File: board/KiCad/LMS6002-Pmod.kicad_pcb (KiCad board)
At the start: 2 copper layers, 30.5 x 29.2 mm, 3 parts, among them P1 PMOD_2x6, P2 PMOD_2x6, U1 iCE40_1K4K_TQ144

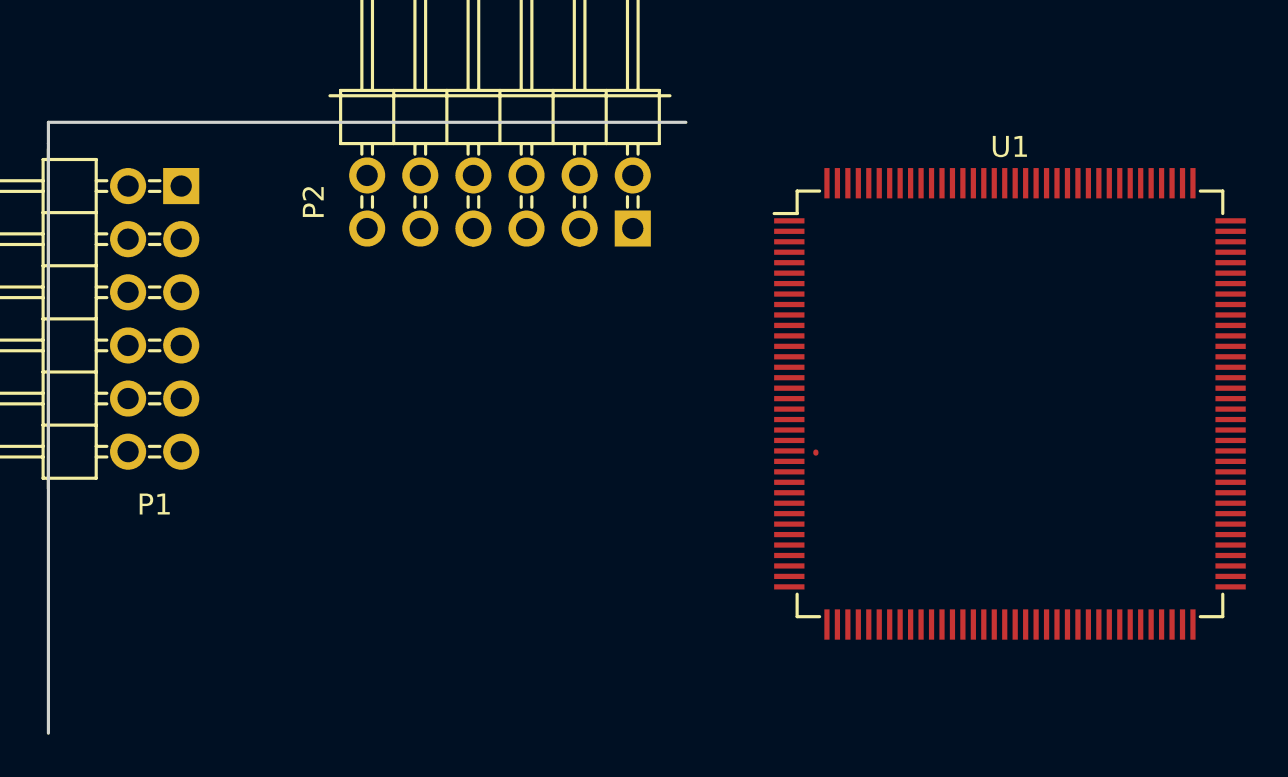
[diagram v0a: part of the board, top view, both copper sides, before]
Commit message: pmod wiring
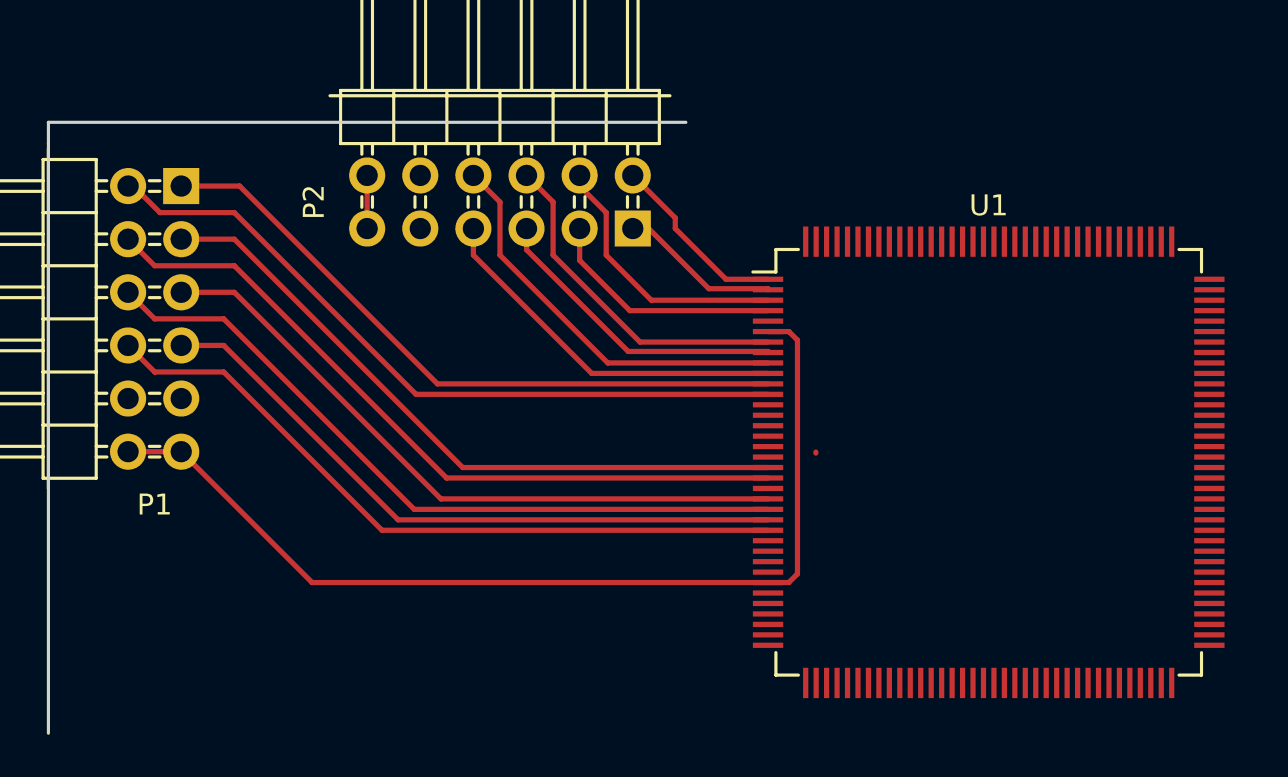
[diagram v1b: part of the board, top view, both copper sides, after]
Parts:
- moved U1 2.97 mm to (133.9, 101.1)
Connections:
- U1 pad 30: Net-(U1-Pad30) -> +3V3
- U1 pad 6: Net-(U1-Pad6) -> +3V3
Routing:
- net +3V3: track 0.00 -> 50.1 mm
- net PIO5: track 0.00 -> 35.3 mm
- net PIO6: track 0.00 -> 34.9 mm
- net PIO4: track 0.00 -> 34.7 mm
- net PIO7: track 0.00 -> 34.3 mm
- net PIO1: track 0.00 -> 32.6 mm
- net PIO2: track 0.00 -> 32.1 mm
- net PIO0: track 0.00 -> 32.0 mm
- net PIO3: track 0.00 -> 31.5 mm
- net PIO15: track 0.00 -> 19.3 mm
- net PIO11: track 0.76 -> 18.5 mm
- net PIO14: track 0.00 -> 16.3 mm
- net PIO10: track 0.64 -> 15.3 mm
- net PIO13: track 0.25 -> 13.2 mm
- net PIO9: track 0.76 -> 12.3 mm
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
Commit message: Finalize first draft
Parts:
- added C1: 10µF, Capacitors_SMD:C_0603_HandSoldering, F.Cu at (117.5, 112.2)
- added C10: 10µF, Capacitors_SMD:C_0603_HandSoldering, B.Cu at (126.8, 96.3)
- added C11: 1µF, Capacitors_SMD:C_0603_HandSoldering, B.Cu at (128.6, 96.3)
- added C12: 0.1µF, Capacitors_SMD:C_0603_HandSoldering, B.Cu at (130.4, 96.3)
- added C13: 0.01µF, Capacitors_SMD:C_0603_HandSoldering, B.Cu at (124.9, 96.3)
- added C14: 100n, Capacitors_SMD:C_0603_HandSoldering, B.Cu at (140.4, 105.8)
- added C15: 100n, Capacitors_SMD:C_0603_HandSoldering, B.Cu at (122.8, 93.9)
- added C16: 100n, Capacitors_SMD:C_0603_HandSoldering, F.Cu at (128.8, 115.3)
- added C17: 100n, Capacitors_SMD:C_0603_HandSoldering, B.Cu at (119.7, 108.7)
- added C18: 100n, Capacitors_SMD:C_0603_HandSoldering, B.Cu at (142.9, 103.7)
- added C19: 100n, Capacitors_SMD:C_0603_HandSoldering, B.Cu at (138.1, 95.9)
- added C2: 0.1µF, Capacitors_SMD:C_0603_HandSoldering, F.Cu at (115.7, 112.2)
- added C20: 100n, Capacitors_SMD:C_0603_HandSoldering, F.Cu at (140.5, 89.6)
- added C21: 100n, Capacitors_SMD:C_0603_HandSoldering, F.Cu at (134.2, 89.6)
- added C22: 100n, Capacitors_SMD:C_0603_HandSoldering, F.Cu at (118.5, 107.7)
- added C23: 100n, Capacitors_SMD:C_0603_HandSoldering, B.Cu at (126.7, 91.5)
- added C3: 1µF, Capacitors_Tantalum_SMD:TantalC_SizeA_EIA-3216_HandSoldering, B.Cu at (109.1, 97.7)
- added C4: 1µF, Capacitors_Tantalum_SMD:TantalC_SizeA_EIA-3216_HandSoldering, B.Cu at (116.8, 109.7)
- added C5: 0.1µ, Capacitors_SMD:C_0603_HandSoldering, B.Cu at (116.3, 102.0)
- added C6: 10µF, Capacitors_SMD:C_0603_HandSoldering, B.Cu at (126.8, 100.5)
- added C7: 1µF, Capacitors_SMD:C_0603_HandSoldering, B.Cu at (128.6, 100.5)
- added C8: 0.1µF, Capacitors_SMD:C_0603_HandSoldering, B.Cu at (124.9, 100.5)
- added C9: 0.01µF, Capacitors_SMD:C_0603_HandSoldering, B.Cu at (130.4, 100.5)
- added CON1: BARREL_JACK, Connect:BARREL_JACK, F.Cu at (105.2, 114.0)
- added D1: 5V-SOD-123F, pmod:SOD-123F_Handsoldering, B.Cu at (96.3, 114.9)
- added D2: Schottky 0520, pmod:SOD-123_Handsoldering, F.Cu at (140.2, 87.6)
- added D3: LED, SMD_Packages:SMD-1206_Pol, F.Cu at (132.8, 87.3)
- added D4: LED, SMD_Packages:SMD-1206_Pol, F.Cu at (127.0, 87.3)
- added D5: LED, SMD_Packages:SMD-1206_Pol, F.Cu at (121.3, 87.3)
- added D6: LED, SMD_Packages:SMD-1206_Pol, F.Cu at (133.0, 119.0)
- added F1: 2A-0603, Capacitors_SMD:C_0603_HandSoldering, B.Cu at (97.4, 107.6)
- added J1: FX10B_80S_8, pmod:FX10B_80S_8, F.Cu at (151.4, 103.0)
- added J2: Pinheader_1x6_TH, Pin_Headers:Pin_Header_Straight_1x06, F.Cu at (113.7, 118.8)
- added J3: SELECT_DIV, Pin_Headers:Pin_Header_Straight_1x03, F.Cu at (104.6, 102.4)
- added JP1: LDO_1V2_IN_SEL, Pin_Headers:Pin_Header_Straight_1x03, F.Cu at (92.3, 112.6)
- added Q1: IRLML6344bpf, TO_SOT_Packages_SMD:SOT-23_Handsoldering, B.Cu at (99.7, 112.0)
- added R1: 100, Resistors_SMD:R_0603_HandSoldering, F.Cu at (113.7, 106.4)
- added R10: 10k, Resistors_SMD:R_0603_HandSoldering, B.Cu at (135.3, 104.3)
- added R11: 10k, Resistors_SMD:R_0603_HandSoldering, F.Cu at (143.3, 115.1)
- added R12: 10K, Resistors_SMD:R_0603_HandSoldering, F.Cu at (143.3, 117.0)
- added R2: 10, Resistors_SMD:R_0603_HandSoldering, F.Cu at (129.0, 89.5)
- added R3: 10, Resistors_SMD:R_0603_HandSoldering, F.Cu at (124.6, 89.5)
- added R4: 10, Resistors_SMD:R_0603_HandSoldering, F.Cu at (120.0, 89.6)
- added R5: R, Resistors_SMD:R_0603_HandSoldering, B.Cu at (112.4, 98.0)
- added R6: 10k, Resistors_SMD:R_0603_HandSoldering, B.Cu at (124.9, 109.2)
- added R7: 10K, Resistors_SMD:R_0603_HandSoldering, F.Cu at (139.0, 116.2)
- added R8: 10, Resistors_SMD:R_0603_HandSoldering, F.Cu at (134.6, 116.2)
- added R9: 10k, Resistors_SMD:R_0603_HandSoldering, B.Cu at (125.0, 104.8)
- added SW1: ICE_RESET, pmod:B3U-1000P_Handsoldering, F.Cu at (141.9, 119.7)
- added U2: LD6815, pmod:SOT-753_(TSOP-5)_Handsoldering, B.Cu at (111.1, 104.4)
- added U3: LTC1799, pmod:TSOT-23_Handsoldering, B.Cu at (117.9, 98.0)
- added U4: N25Q, pmod:SOP2-8_Handsoldering, B.Cu at (131.9, 108.0)
- moved U1 2.57 mm to (131.7, 102.5)
- moved P2 1.61 mm to (116.6, 83.0)
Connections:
- P1 pad 12: +3V3 -> 3V3_PMOD
- P1 pad 6: +3V3 -> 3V3_PMOD
- P2 pad 12: +3V3 -> 3V3_PMOD
- P2 pad 6: +3V3 -> 3V3_PMOD
- U1 pad 100: Net-(U1-Pad100) -> 3V3_PMOD
- U1 pad 101: Net-(U1-Pad101) -> FCLK2
- U1 pad 102: Net-(U1-Pad102) -> RFDIO_GPIO0
- U1 pad 103: Net-(U1-Pad103) -> GND
- U1 pad 104: Net-(U1-Pad104) -> RFDIO_GPIO1
- U1 pad 105: Net-(U1-Pad105) -> RFDIO_GPIO2
- U1 pad 106: Net-(U1-Pad106) -> RFDIO_REF_CLK_IN
- U1 pad 107: Net-(U1-Pad107) -> TXEN
- U1 pad 108: Net-(U1-Pad108) -> (no net)
- U1 pad 110: Net-(U1-Pad110) -> (no net)
- U1 pad 111: Net-(U1-Pad111) -> 1V2_LDO
- U1 pad 112: Net-(U1-Pad112) -> RXEN
- U1 pad 113: Net-(U1-Pad113) -> RFDIO_SPI_EN
- U1 pad 114: Net-(U1-Pad114) -> RFDIO_SPI_CLK
- U1 pad 115: Net-(U1-Pad115) -> RFDIO_SPI_MISO
- U1 pad 116: Net-(U1-Pad116) -> RFDIO_SPI_MOSI
- U1 pad 117: Net-(U1-Pad117) -> RFDIO_RESET
- U1 pad 118: Net-(U1-Pad118) -> FCLK1
- U1 pad 119: Net-(U1-Pad119) -> DIQ2_D11
- U1 pad 120: Net-(U1-Pad120) -> DIQ2_D9
- U1 pad 121: Net-(U1-Pad121) -> DIQ2_D7
- U1 pad 122: Net-(U1-Pad122) -> DIQ2_D5
- U1 pad 123: Net-(U1-Pad123) -> 3V3_PMOD
- U1 pad 124: Net-(U1-Pad124) -> (no net)
- U1 pad 125: Net-(U1-Pad125) -> (no net)
- U1 pad 126: Net-(U1-Pad126) -> (no net)
- U1 pad 127: Net-(U1-Pad127) -> (no net)
- U1 pad 128: Net-(U1-Pad128) -> DIQ2_D3
- U1 pad 129: Net-(U1-Pad129) -> DIQ2_D1
- U1 pad 13: Net-(U1-Pad13) -> GND
- U1 pad 130: Net-(U1-Pad130) -> (no net)
- U1 pad 131: Net-(U1-Pad131) -> (no net)
- U1 pad 132: Net-(U1-Pad132) -> GND
- U1 pad 133: Net-(U1-Pad133) -> 3V3_PMOD
- U1 pad 134: Net-(U1-Pad134) -> DIQ1_D11
- U1 pad 135: Net-(U1-Pad135) -> (no net)
- U1 pad 136: Net-(U1-Pad136) -> (no net)
- U1 pad 137: Net-(U1-Pad137) -> (no net)
- U1 pad 138: Net-(U1-Pad138) -> (no net)
- U1 pad 139: Net-(U1-Pad139) -> (no net)
- U1 pad 14: Net-(U1-Pad14) -> GND
- U1 pad 140: Net-(U1-Pad140) -> GND
- U1 pad 141: Net-(U1-Pad141) -> (no net)
- U1 pad 15: Net-(U1-Pad15) -> (no net)
- U1 pad 16: Net-(U1-Pad16) -> (no net)
- U1 pad 17: Net-(U1-Pad17) -> (no net)
- U1 pad 18: Net-(U1-Pad18) -> (no net)
- U1 pad 21: Net-(U1-Pad21) -> ICE_CLK_IN
- U1 pad 26: Net-(U1-Pad26) -> (no net)
- U1 pad 27: Net-(U1-Pad27) -> 1V2_LDO
- U1 pad 28: Net-(U1-Pad28) -> (no net)
- U1 pad 29: Net-(U1-Pad29) -> (no net)
- U1 pad 30: +3V3 -> 3V3_PMOD
- U1 pad 31: Net-(U1-Pad31) -> (no net)
- U1 pad 32: Net-(U1-Pad32) -> (no net)
- U1 pad 33: Net-(U1-Pad33) -> (no net)
- U1 pad 34: Net-(U1-Pad34) -> (no net)
- U1 pad 37: Net-(U1-Pad37) -> (no net)
- U1 pad 38: Net-(U1-Pad38) -> (no net)
- U1 pad 39: Net-(U1-Pad39) -> (no net)
- U1 pad 40: Net-(U1-Pad40) -> (no net)
- U1 pad 41: Net-(U1-Pad41) -> (no net)
- U1 pad 42: Net-(U1-Pad42) -> (no net)
- U1 pad 43: Net-(U1-Pad43) -> (no net)
- U1 pad 44: Net-(U1-Pad44) -> (no net)
- U1 pad 45: Net-(U1-Pad45) -> (no net)
- U1 pad 46: Net-(U1-Pad46) -> (no net)
- U1 pad 47: Net-(U1-Pad47) -> (no net)
- U1 pad 48: Net-(U1-Pad48) -> (no net)
- U1 pad 49: Net-(U1-Pad49) -> (no net)
- U1 pad 5: Net-(U1-Pad5) -> GND
- U1 pad 50: Net-(U1-Pad50) -> (no net)
- U1 pad 51: Net-(U1-Pad51) -> 1V2_LDO
- U1 pad 52: Net-(U1-Pad52) -> (no net)
- U1 pad 53: Net-(U1-Pad53) -> (no net)
- U1 pad 54: Net-(U1-Pad54) -> (no net)
- U1 pad 55: Net-(U1-Pad55) -> (no net)
- U1 pad 56: Net-(U1-Pad56) -> (no net)
- U1 pad 57: Net-(U1-Pad57) -> (no net)
- U1 pad 58: Net-(U1-Pad58) -> (no net)
- U1 pad 59: Net-(U1-Pad59) -> GND
- U1 pad 6: +3V3 -> 3V3_PMOD
- U1 pad 60: Net-(U1-Pad60) -> (no net)
- U1 pad 61: Net-(U1-Pad61) -> (no net)
- U1 pad 62: Net-(U1-Pad62) -> (no net)
- U1 pad 63: Net-(U1-Pad63) -> (no net)
- U1 pad 64: Net-(U1-Pad64) -> (no net)
- U1 pad 65: Net-(U1-Pad65) -> ICE_CDONE
- U1 pad 66: Net-(U1-Pad66) -> ICE_CRESET_B
- U1 pad 67: Net-(U1-Pad67) -> EXT_SPI_MOSI
- U1 pad 68: Net-(U1-Pad68) -> EXT_SPI_MISO
- U1 pad 69: Net-(U1-Pad69) -> GND
- U1 pad 70: Net-(U1-Pad70) -> EXT_SPI_CLK
- U1 pad 71: Net-(U1-Pad71) -> EXT_SPI_SS_B
- U1 pad 72: Net-(U1-Pad72) -> 3V3_PMOD
- U1 pad 73: Net-(U1-Pad73) -> DIQ1_D1
- U1 pad 74: Net-(U1-Pad74) -> DIQ1_D3
- U1 pad 75: Net-(U1-Pad75) -> DIQ1_D5
- U1 pad 76: Net-(U1-Pad76) -> DIQ1_D7
- U1 pad 77: Net-(U1-Pad77) -> (no net)
- U1 pad 78: Net-(U1-Pad78) -> DIQ1_SEL
- U1 pad 79: Net-(U1-Pad79) -> DIQ1_D0
- U1 pad 80: Net-(U1-Pad80) -> DIQ1_D2
- U1 pad 81: Net-(U1-Pad81) -> DIQ1_D4
- U1 pad 82: Net-(U1-Pad82) -> (no net)
- U1 pad 83: Net-(U1-Pad83) -> (no net)
- U1 pad 84: Net-(U1-Pad84) -> (no net)
- U1 pad 85: Net-(U1-Pad85) -> (no net)
- U1 pad 86: Net-(U1-Pad86) -> GND
- U1 pad 87: Net-(U1-Pad87) -> DIQ1_D6
- U1 pad 88: Net-(U1-Pad88) -> DIQ1_D8
- U1 pad 89: Net-(U1-Pad89) -> 3V3_PMOD
- U1 pad 90: Net-(U1-Pad90) -> DIQ1_D10
- U1 pad 91: Net-(U1-Pad91) -> DIQ1_D9
- U1 pad 92: Net-(U1-Pad92) -> 1V2_LDO
- U1 pad 93: Net-(U1-Pad93) -> DIQ2_SEL
- U1 pad 94: Net-(U1-Pad94) -> DIQ2_D0
- U1 pad 95: Net-(U1-Pad95) -> DIQ2_D2
- U1 pad 96: Net-(U1-Pad96) -> DIQ2_D4
- U1 pad 97: Net-(U1-Pad97) -> DIQ2_D6
- U1 pad 98: Net-(U1-Pad98) -> DIQ2_D8
- U1 pad 99: Net-(U1-Pad99) -> DIQ2_D10
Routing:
- net GND: track 0.00 -> 204.9 mm, vias 0 -> 9
- net 3V3_PMOD: track 0.00 -> 178.9 mm, vias 0 -> 5
- net 1V2_LDO: track 0.00 -> 94.5 mm, vias 0 -> 6
- net 5V: track 0.00 -> 83.3 mm, vias 0 -> 1
- net +3V3: track 50.1 -> 0.00 mm
- net 5V_LDO_IN: track 0.00 -> 41.5 mm
- net DIQ1_D11: track 0.00 -> 34.2 mm, vias 0 -> 2
- net EXT_SPI_SS_B: track 0.00 -> 34.0 mm, vias 0 -> 1
- net EXT_SPI_CLK: track 0.00 -> 32.7 mm, vias 0 -> 1
- net DIQ2_D1: track 0.00 -> 30.8 mm, vias 0 -> 2
- net EXT_SPI_MISO: track 0.00 -> 30.8 mm, vias 0 -> 1
- net DIQ2_D3: track 0.00 -> 29.8 mm, vias 0 -> 2
- net DIQ2_D5: track 0.00 -> 27.6 mm, vias 0 -> 2
- net DIQ2_D7: track 0.00 -> 26.6 mm, vias 0 -> 2
- net EXT_SPI_MOSI: track 0.00 -> 26.3 mm, vias 0 -> 1
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- added copper zone on B.Cu, net GND
- added copper zone on F.Cu, net GND
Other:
- board size 30.5 x 29.2 mm -> 70.6 x 36.8 mm
- net class Default: clearance 0.2 -> 0.1524
- net class SeeedMinimum added: clearance 0.1524, trace_width 0.1524, via_dia 0.6, via_drill 0.3
- rule trace_clearance: 0.2 -> 0.1524
- rule trace_min: 0.2 -> 0.1524

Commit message: Improve P&R
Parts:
- moved C12 29.5 mm to (101.1, 92.5), turned to 180 degrees
- moved C11 27.6 mm to (101.1, 94.2), turned to 180 degrees
- moved C10 25.7 mm to (101.1, 96.0), turned to 180 degrees
- moved C13 23.8 mm to (101.1, 97.8), turned to 180 degrees
- moved R9 8.29 mm to (121.8, 112.5), turned to 0 degrees
- moved C9 6.44 mm to (124.6, 103.3), turned to 90 degrees
- moved C6 6.44 mm to (121.0, 103.3), turned to 90 degrees
- moved C7 6.44 mm to (122.8, 103.3), turned to 90 degrees
- moved C8 6.35 mm to (119.2, 103.3), turned to 90 degrees
- moved R6 6.09 mm to (121.8, 114.4), turned to 0 degrees
- moved SW1 5.24 mm to (136.8, 118.5), turned to 180 degrees
- moved R10 2.92 mm to (132.4, 104.2), turned to 0 degrees
- moved D6 2.84 mm to (130.8, 117.2), turned to 90 degrees
- moved C16 1.51 mm to (127.3, 115.1)
- moved R11 1.40 mm to (144.7, 115.1)
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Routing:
- net GND: track 204.9 -> 272.1 mm, vias 9 -> 16
- net 5V: track 83.3 -> 97.6 mm, vias 1 -> 2
- net EXT_SPI_SS_B: track 34.0 -> 41.9 mm, vias 1 -> 2
- net 3V3_PMOD: track 178.9 -> 186.4 mm
- net 1V2_LDO: track 94.5 -> 87.3 mm, vias 6 -> 5
- net Net-(R9-Pad2): track 4.04 -> 9.21 mm
- net EXT_SPI_MOSI: track 26.3 -> 30.2 mm
- net EXT_SPI_MISO: track 30.8 -> 34.4 mm, vias 1 -> 2
- net EXT_SPI_CLK: track 32.7 -> 35.6 mm
- net Net-(R10-Pad2): track 4.94 -> 6.74 mm, vias 0 -> 2
- net ICE_CRESET_B: track 13.4 -> 11.9 mm
- net ICE_CLK_IN: track 7.28 -> 8.37 mm
- net (no net): track 0.78 -> 0.00 mm

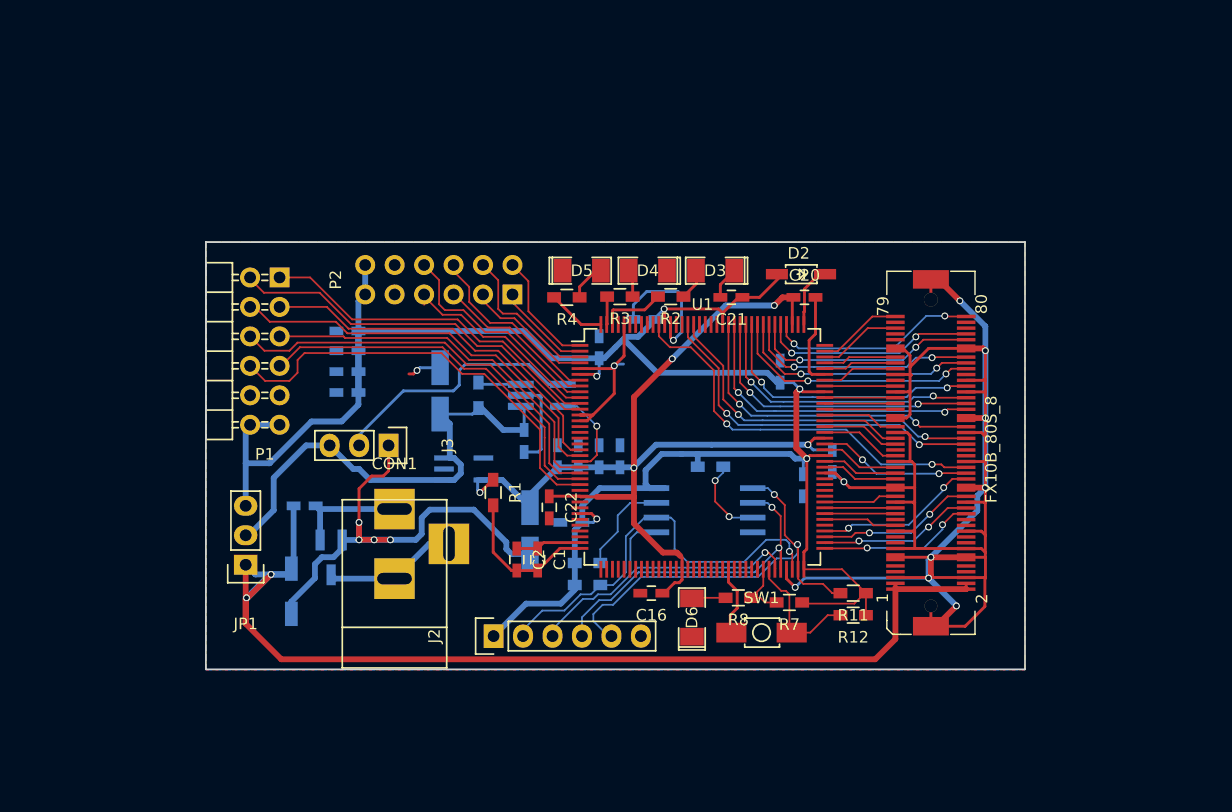
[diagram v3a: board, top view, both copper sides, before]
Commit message: Improve design
* PMOS on input voltage for polarity
* Re-design board to add mount holes and better routing
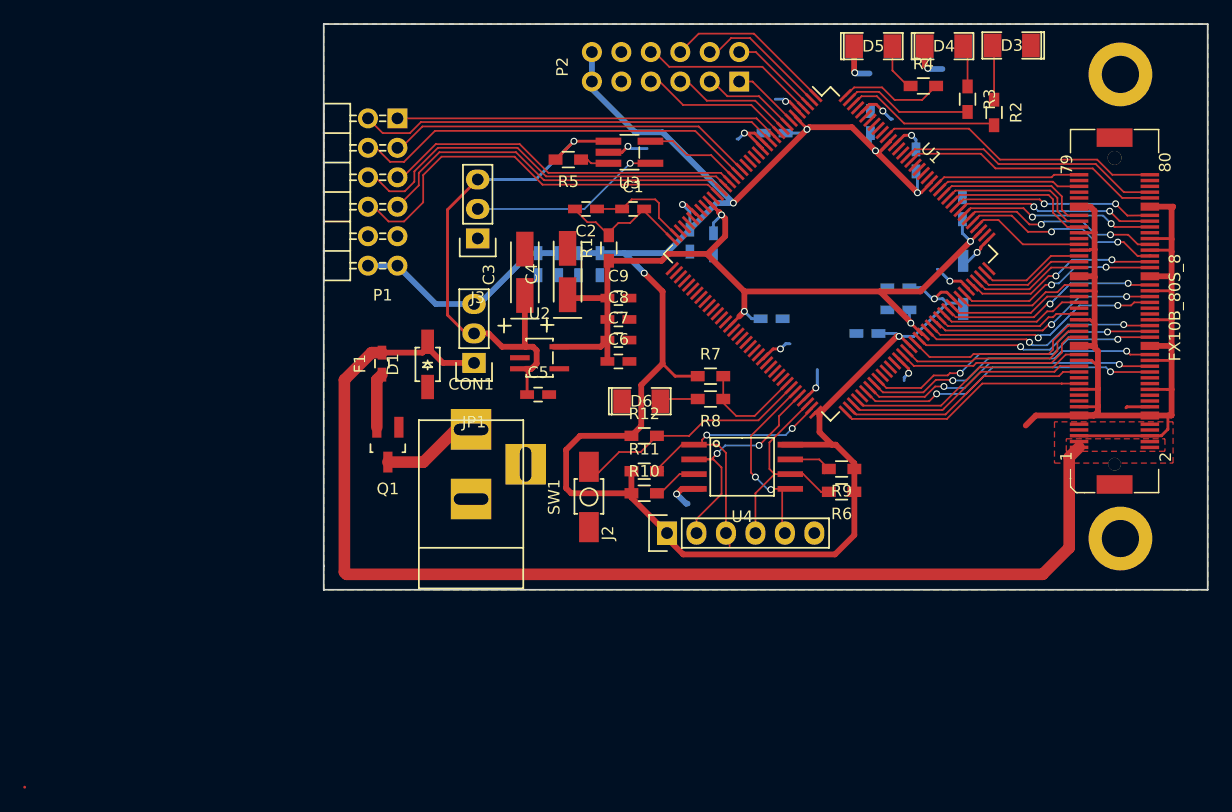
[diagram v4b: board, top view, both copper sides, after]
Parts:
- added P3: Myriad_Mount_Hole, pmod:Myriad_Mount_Hole, F.Cu at (171.8, 71.0)
- added P4: Myriad_Mount_Hole, pmod:Myriad_Mount_Hole, F.Cu at (171.1, 110.4)
- C16, C20, C21, C22, D2: moved to B.Cu
- C3, C4, C5, C6, C7, C8, C9, D1, F1, R10, R5, R6, R9, U2, U3, U4: moved to F.Cu
- Q1: value IRLML6344bpf -> Q_PMOS_GSD; moved to F.Cu
- moved R4 35.7 mm to (150.7, 71.4), turned to 0 degrees
- moved C17 34.7 mm to (148.6, 88.8)
- moved R3 34.5 mm to (154.6, 72.5), turned to 270 degrees
- moved D3 32.1 mm to (158.4, 67.9)
- moved R2 32.1 mm to (156.8, 73.7), turned to 270 degrees
- moved D4 32.0 mm to (152.5, 67.9), turned to 0 degrees
- moved C14 31.8 mm to (146.2, 74.5), turned to 90 degrees
- moved D5 31.7 mm to (146.4, 67.9)
- moved C15 31.7 mm to (150.1, 77.8)
- moved C1 31.3 mm to (125.7, 82.0), turned to 0 degrees
- moved C2 30.8 mm to (121.7, 82.0), turned to 180 degrees
- moved P2 26.8 mm to (136.1, 64.6)
- moved C22 26.7 mm to (132.7, 85.0)
- moved JP1 26.3 mm to (112.0, 95.2)
- moved C16 25.8 mm to (137.7, 91.4), turned to 0 degrees
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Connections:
- CON1 pad 1: Net-(CON1-Pad1) -> /power_supply/VIN
- CON1 pad 2: Net-(CON1-Pad2) -> GND
- CON1 pad 3: Net-(CON1-Pad2) -> GND
- F1 pad 1: Net-(CON1-Pad1) -> /power_supply/VIN_PROT
- J2 pad 2: EXT_SPI_CLK -> EXT_SPI_MISO
- J2 pad 3: EXT_SPI_MOSI -> EXT_SPI_SS_B
- J2 pad 4: EXT_SPI_MISO -> EXT_SPI_CLK
- J2 pad 5: EXT_SPI_SS_B -> EXT_SPI_MOSI
- Q1 pad 1: Net-(CON1-Pad1) -> GND
- Q1 pad 2: GND -> /power_supply/VIN_PROT
- Q1 pad 3: Net-(CON1-Pad2) -> /power_supply/VIN
- U1 pad 1: PIO12 -> PIO14
- U1 pad 101: FCLK2 -> DIQ2_D4
- U1 pad 102: RFDIO_GPIO0 -> DIQ2_D7
- U1 pad 104: RFDIO_GPIO1 -> DIQ2_D9
- U1 pad 105: RFDIO_GPIO2 -> DIQ2_D6
- U1 pad 106: RFDIO_REF_CLK_IN -> DIQ2_D8
- U1 pad 107: TXEN -> DIQ2_D10
- U1 pad 112: RXEN -> FCLK2
- U1 pad 113: RFDIO_SPI_EN -> DIQ2_D11
- U1 pad 114: RFDIO_SPI_CLK -> FCLK1
- U1 pad 115: RFDIO_SPI_MISO -> RFDIO_RESET
- U1 pad 117: RFDIO_RESET -> RFDIO_SPI_MISO
- U1 pad 118: FCLK1 -> RFDIO_GPIO0
- U1 pad 119: DIQ2_D11 -> RFDIO_GPIO1
- U1 pad 120: DIQ2_D9 -> RFDIO_GPIO2
- U1 pad 121: DIQ2_D7 -> RFDIO_REF_CLK_IN
- U1 pad 122: DIQ2_D5 -> TXEN
- U1 pad 128: DIQ2_D3 -> RFDIO_SPI_CLK
- U1 pad 129: DIQ2_D1 -> RFDIO_SPI_EN
- U1 pad 134: DIQ1_D11 -> RXEN
- U1 pad 2: PIO8 -> PIO13
- U1 pad 3: PIO13 -> PIO12
- U1 pad 4: PIO9 -> PIO15
- U1 pad 7: PIO14 -> PIO8
- U1 pad 73: DIQ1_D1 -> DIQ1_SEL
- U1 pad 74: DIQ1_D3 -> DIQ1_D0
- U1 pad 75: DIQ1_D5 -> DIQ1_D2
- U1 pad 76: DIQ1_D7 -> DIQ1_D4
- U1 pad 78: DIQ1_SEL -> DIQ1_D1
- U1 pad 79: DIQ1_D0 -> DIQ1_D3
- U1 pad 8: PIO10 -> PIO9
- U1 pad 80: DIQ1_D2 -> DIQ1_D5
- U1 pad 81: DIQ1_D4 -> DIQ1_D7
- U1 pad 9: PIO15 -> PIO10
- U1 pad 93: DIQ2_SEL -> DIQ1_D11
- U1 pad 94: DIQ2_D0 -> DIQ2_D1
- U1 pad 95: DIQ2_D2 -> DIQ2_D3
- U1 pad 96: DIQ2_D4 -> DIQ2_SEL
- U1 pad 97: DIQ2_D6 -> DIQ2_D0
- U1 pad 98: DIQ2_D8 -> DIQ2_D5
- U1 pad 99: DIQ2_D10 -> DIQ2_D2
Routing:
- net GND: track 272.1 -> 134.9 mm, vias 16 -> 12
- net EXT_SPI_SS_B: track 41.9 -> 26.3 mm
- net DIQ1_D0: track 6.09 -> 21.5 mm
- net DIQ1_SEL: track 6.30 -> 21.7 mm
- net EXT_SPI_CLK: track 35.6 -> 20.3 mm, vias 1 -> 0
- net DIQ1_D2: track 6.09 -> 21.2 mm
- net 3V3_PMOD: track 186.4 -> 201.4 mm, vias 5 -> 8
- net DIQ1_D4: track 6.29 -> 21.1 mm
- net EXT_SPI_MISO: track 34.4 -> 19.8 mm
- net EXT_SPI_MOSI: track 30.2 -> 15.8 mm, vias 1 -> 2
- net DIQ1_D11: track 34.2 -> 20.5 mm
- net DIQ1_D1: track 13.7 -> 26.2 mm
- net DIQ1_D3: track 13.5 -> 25.9 mm
- net DIQ1_D5: track 13.6 -> 26.0 mm
- net Net-(CON1-Pad2): track 11.5 -> 0.00 mm
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- added copper zone on F.Cu, net 5V
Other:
- board size 70.6 x 36.8 mm -> 76.2 x 48.8 mm

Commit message: Add OSHW Logo
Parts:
- added T1: OSHW_Logo, Symbols:Symbol_OSHW-Logo_SilkScreen, F.Cu at (153.8, 103.6)
